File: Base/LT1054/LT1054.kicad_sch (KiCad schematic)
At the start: 41 parts, among them J1 Barrel_Jack_Switch, J2 Ground, J3 Conn_01x03_Pin, J4 Conn_01x03_Pin, J5 AudioJack2_Ground, J6 AudioJack2_Ground, Q1 BC846, Q2 40V, U1 LT1054, U2 OPA1656

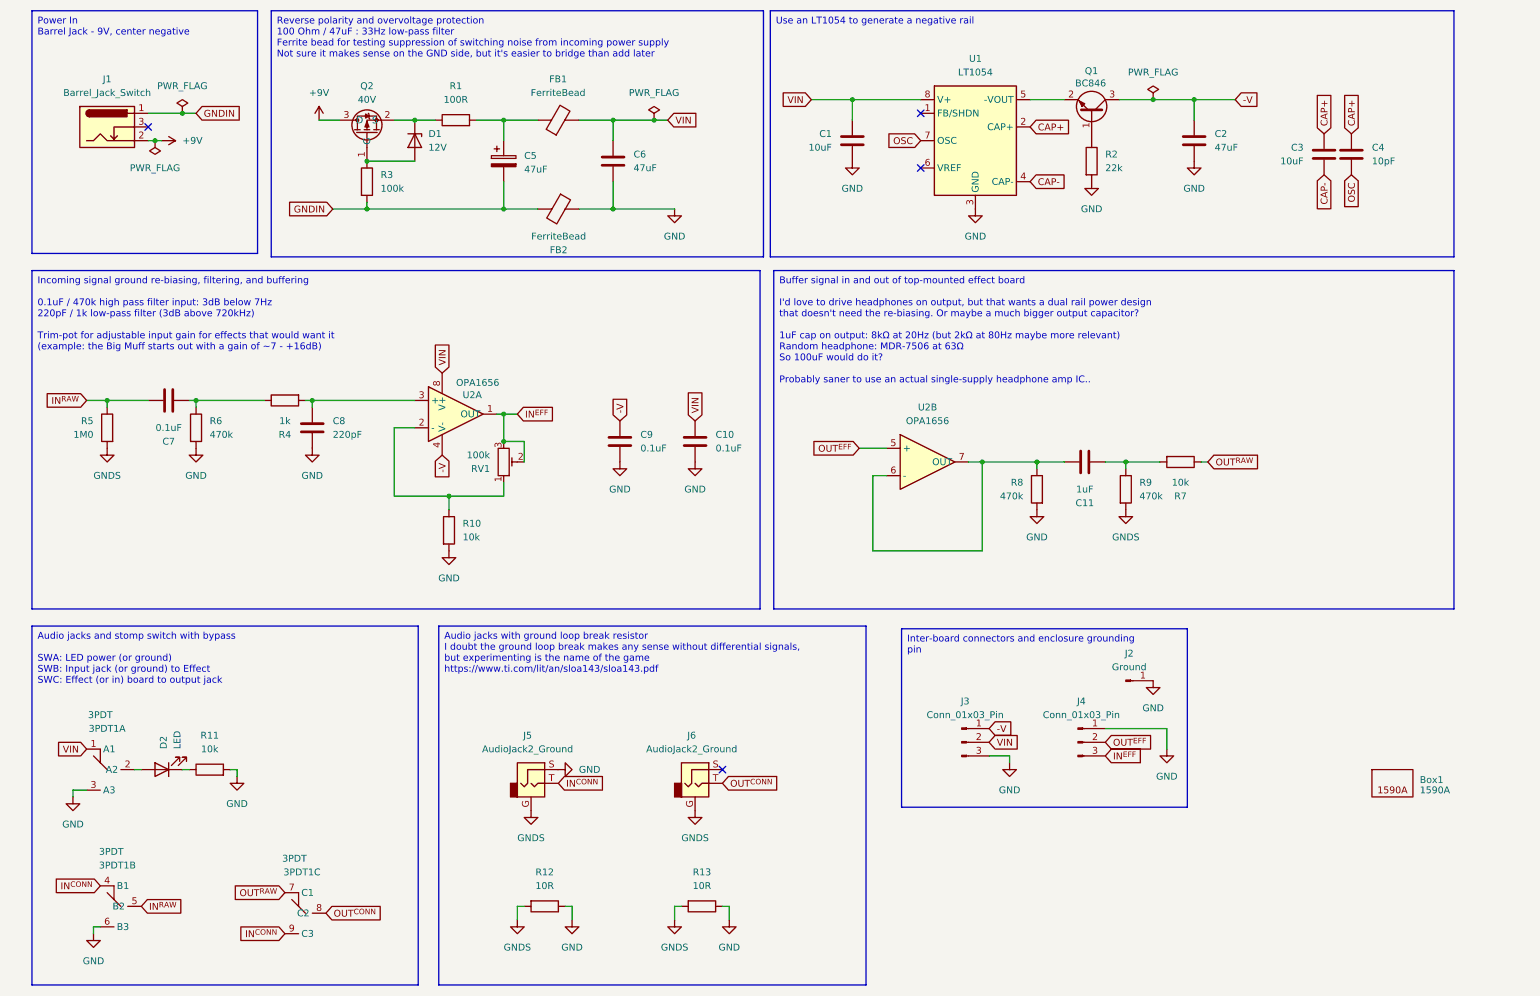
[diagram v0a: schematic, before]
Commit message: Add back the BUF634A to the audio output
With the dual rails, we don't need to have the output capacitor to
rebase the signal levels, and can drive it directly.  Which allows going
back to the headphone amplifier setup using the BUF634A.

Is this a good idea? I dunno.  Having a separate headphone amplifier
makes more sense, I guess, but I liked just being able to connect the
headphones to test things out.

And it's not like these boards make sense for anybody else anyway, so...

Signed-off-by: Linus Torvalds <torvalds@linux-foundation.org>
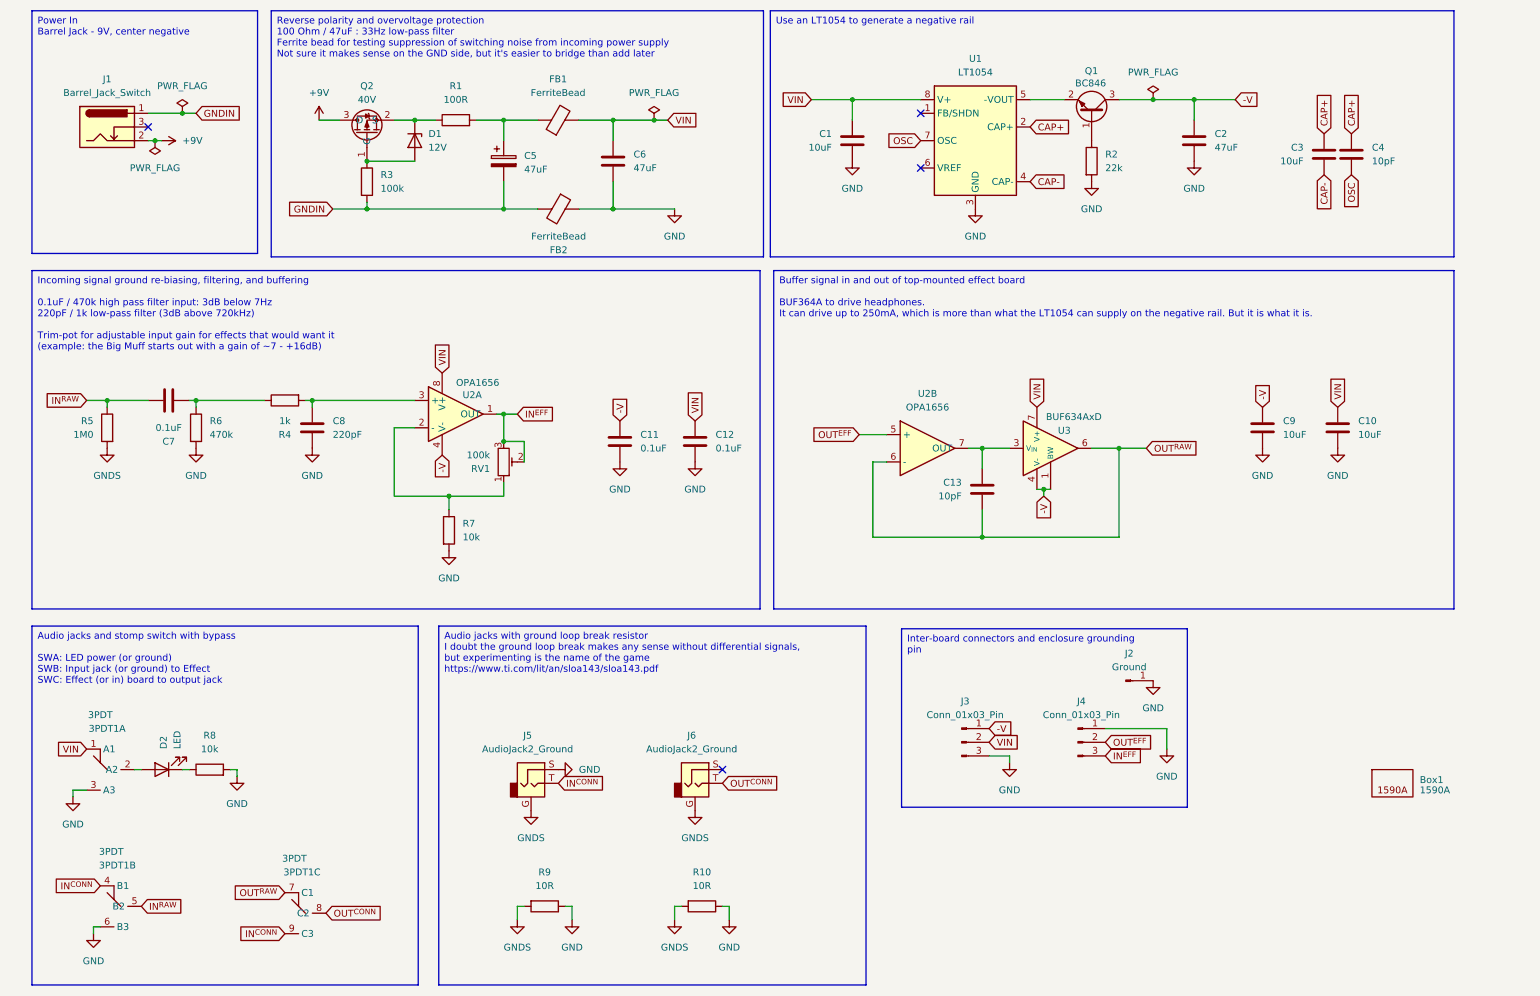
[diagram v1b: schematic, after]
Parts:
- removed C11: 1uF, Capacitor_SMD:C_1206_3216Metric_Pad1.33x1.80mm_HandSolder, symbol Device:C
- removed R7: 10k, Resistor_SMD:R_0805_2012Metric_Pad1.20x1.40mm_HandSolder, symbol Device:R
- removed R8, R9: 470k, Resistor_SMD:R_0805_2012Metric_Pad1.20x1.40mm_HandSolder, symbol Device:R
- added C10, C9: 10uF, Capacitor_SMD:C_1206_3216Metric_Pad1.33x1.80mm_HandSolder, symbol Device:C
- added C13: 10pF, Capacitor_SMD:C_0805_2012Metric_Pad1.18x1.45mm_HandSolder, symbol Device:C
- added U3: BUF634AxD, Package_SO:SOIC-8_3.9x4.9mm_P1.27mm, symbol Amplifier_Buffer:BUF634AxD
- renumbered C9 to C11, C10 to C12, R13 to R10, R10 to R7, R11 to R8, R12 to R9
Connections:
- net -V: now also C9.1, U3.1 (BW), U3.4 (V-)
- net GND: now also C10.2, C9.2
- net OUT^{RAW}: now also U2.6 (-), C13.2, U3.6
- net VIN: now also C10.1, U3.7 (V+)
- net at U2.7 (OUT): now also C13.1, U3.3 (V_{IN}); no longer U2.6 (-)
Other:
- moved on the sheet: U2B
